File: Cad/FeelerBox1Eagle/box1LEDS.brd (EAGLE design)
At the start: 45 x 70 mm, 20 parts, among them Q3 2N2222A, Q4 2N2222A, Q5 2N2222A, X2 87758-0216

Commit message: fixes0.1
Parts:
- removed CN2: (no value), con-hdrs40:70543-03
- removed Q3, Q4, Q5: 2N2222A, transistor-npn:TO18
- removed R4, R5, R6: (no value), SparkFun-Passives:AXIAL-0.4
- removed X2: 87758-0216, con-molex:87758-0216
- added CN1: (no value), con-hdrs40:SIP-100-2V
- moved R2 22.2 mm to (15.2, 57.1), turned to 90 degrees
- moved R1 13.7 mm to (22.9, 57.1), turned to 90 degrees
- moved R3 6.48 mm to (29.2, 57.1), turned to 90 degrees
- moved U$4 2.54 mm to (22.9, 25.4)
- moved U$5 2.54 mm to (15.2, 25.4)
- moved U$6 2.54 mm to (29.2, 25.4)
- moved U$1 2.54 mm to (22.9, 36.8)
- moved U$2 2.54 mm to (15.2, 36.8)
- moved U$3 2.54 mm to (29.2, 36.8)
- moved U$7 2.54 mm to (22.9, 47.0)
- moved U$8 2.54 mm to (15.2, 47.0)
- moved U$9 2.54 mm to (29.2, 47.0)
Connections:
- removed net D11: CN2.3, R6.P$1
- removed net D13: CN2.1, R4.P$2
- removed net N$29: Q3.3, U$6.1
- removed net N$31: Q4.3, U$5.1
- removed net N$32: Q5.3, U$4.1
- removed net N$6: Q3.1, Q4.1, Q5.1, X2.2
- removed net N$7: Q4.2, R5.P$2
- removed net N$8: CN2.2, R5.P$1
- removed net N$9: Q5.2, R4.P$1
- net N$4: now also CN1.2, U$4.1, U$5.1, U$6.1; no longer Q3.2, R6.P$2
- net N$5: now also CN1.1; no longer X2.1
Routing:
- net N$6: track 106.7 -> 0.00 mm
- net N$5: track 53.5 -> 17.8 mm
- net N$9: track 25.8 -> 0.00 mm
- net N$2: track 23.8 -> 0.00 mm
- net N$7: track 19.1 -> 0.00 mm
- net N$3: track 14.7 -> 0.00 mm
- net N$1: track 8.19 -> 0.00 mm
- net N$32: track 6.11 -> 0.00 mm
- net D13: track 5.66 -> 0.00 mm
- net N$4: track 40.5 -> 46.1 mm
- net N$31: track 5.20 -> 0.00 mm
- net N$29: track 5.20 -> 0.00 mm
- net D11: track 4.34 -> 0.00 mm
- net N$8: track 4.34 -> 0.00 mm

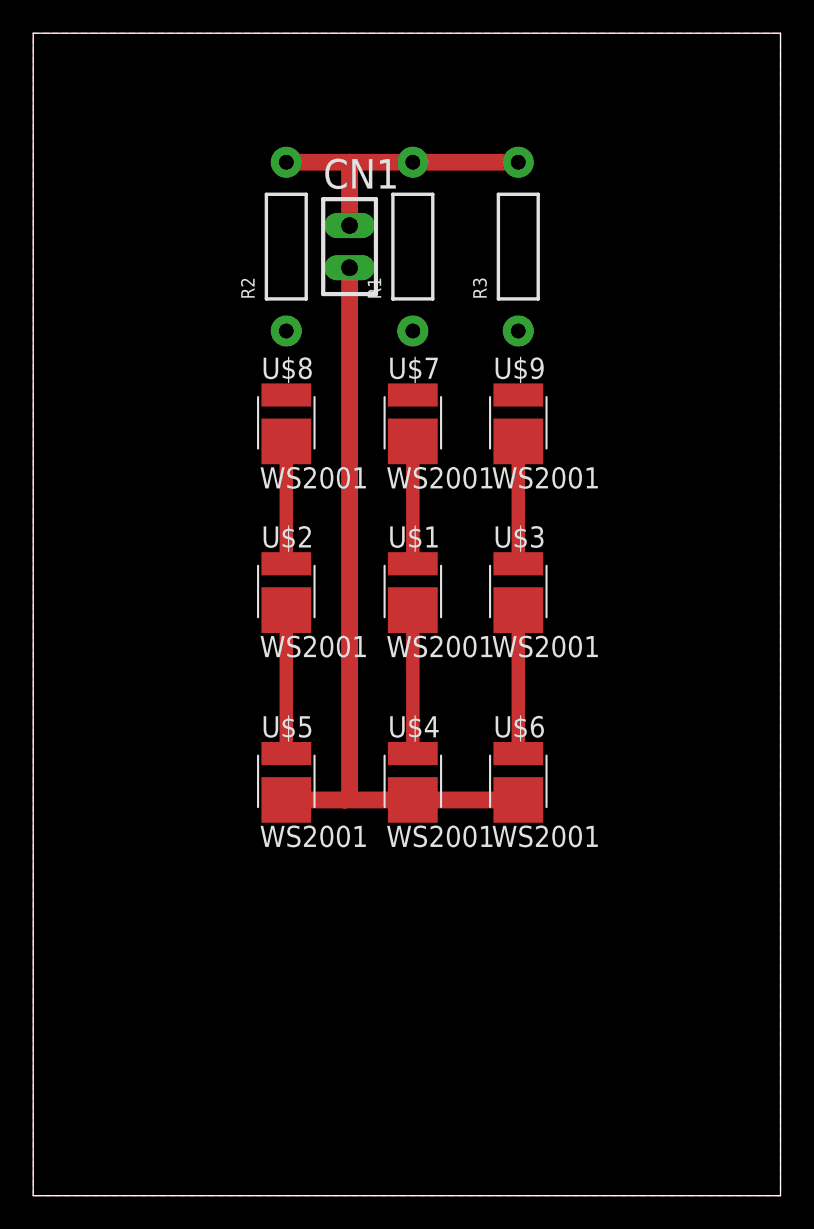
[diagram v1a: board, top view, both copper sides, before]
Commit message: fixes
Fixes, and made made box1Ledboard smaller to improve wifi signal
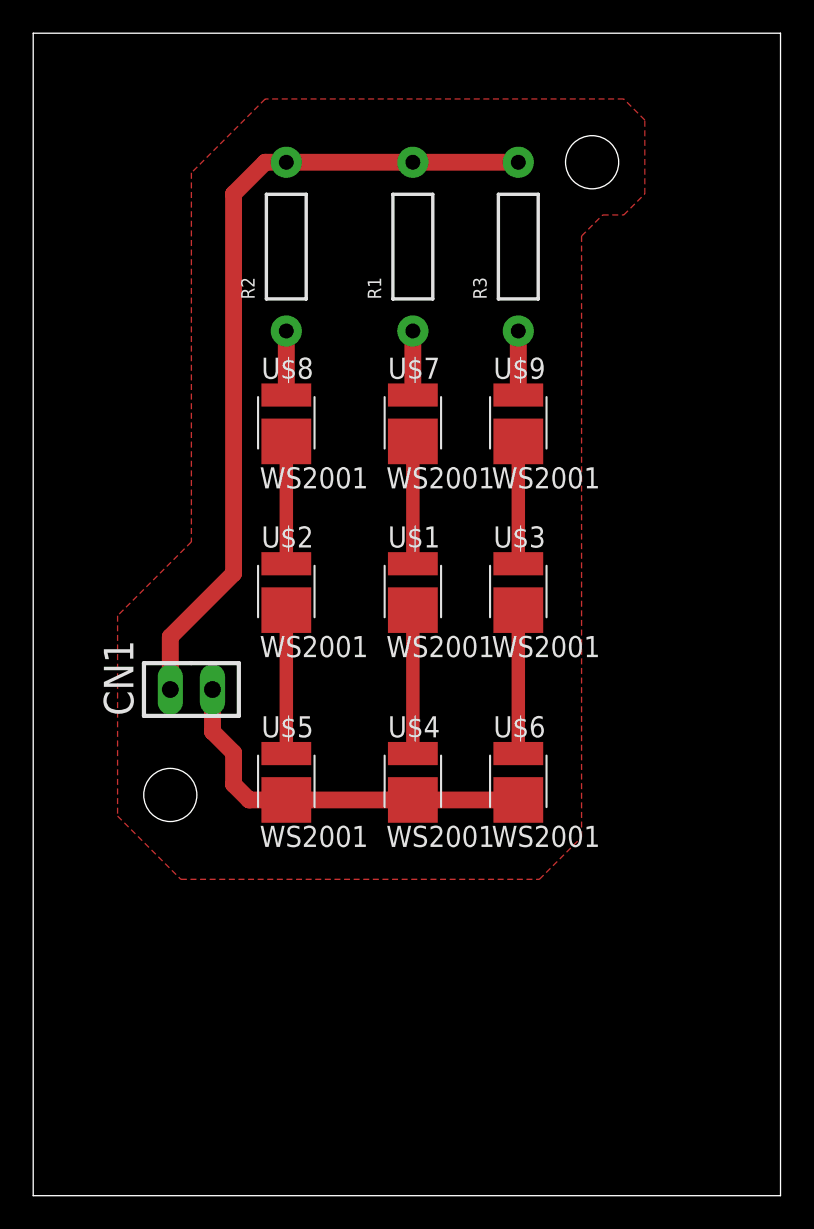
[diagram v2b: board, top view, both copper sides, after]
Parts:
- moved CN1 28.3 mm to (9.53, 30.5), turned to 0 degrees
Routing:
- net N$5: track 17.8 -> 49.4 mm
- net N$4: track 46.1 -> 23.8 mm
- net N$3: track 0.00 -> 3.86 mm
- net N$2: track 0.00 -> 3.86 mm
- net N$1: track 0.00 -> 3.86 mm
- added copper zone on layer 1, net N$6
- removed copper zone on layer 1, net N$10

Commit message: updates
bah
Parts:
- moved CN1 31.0 mm to (21.6, 59.1)
- moved U$5 24.8 mm to (28.6, 46.4)
- moved U$9 21.7 mm to (15.9, 29.8)
- moved U$4 13.9 mm to (28.6, 38.1)
- moved U$2 12.2 mm to (22.9, 46.4)
- moved U$7 11.3 mm to (15.9, 38.1)
- moved U$3 9.44 mm to (22.9, 29.8)
- moved R3 5.43 mm to (24.1, 55.2), turned to 180 degrees
- moved R1 5.24 mm to (24.1, 52.1), turned to 180 degrees
- moved U$6 4.49 mm to (28.6, 29.8)
- moved R2 1.80 mm to (16.5, 55.9)
- moved U$1 1.27 mm to (22.9, 38.1)
- moved U$8 0.90 mm to (15.9, 46.4)
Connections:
- removed net N$20: U$1.2, U$7.1
- removed net N$21: U$2.2, U$8.1
- removed net N$22: U$3.2, U$9.1
- removed net N$23: U$3.1, U$6.2
- removed net N$24: U$2.1, U$5.2
- removed net N$25: U$1.1, U$4.2
- removed net N$4: CN1.2, U$4.1, U$5.1, U$6.1
- new net GND: CN1.2, U$1.1, U$2.1, U$3.1, U$4.1, U$5.1, U$6.1, U$7.1, U$8.1, U$9.1
- net N$1: now also U$3.2, U$6.2
- net N$2: now also U$2.2, U$5.2
- net N$3: now also U$1.2, U$4.2
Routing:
- net GND: track 0.00 -> 93.9 mm
- net N$1: track 3.86 -> 42.5 mm
- net N$5: track 49.4 -> 12.5 mm
- net N$3: track 3.86 -> 28.0 mm
- net N$4: track 23.8 -> 0.00 mm
- net N$2: track 3.86 -> 16.2 mm
- net N$25: track 8.64 -> 0.00 mm
- net N$24: track 8.64 -> 0.00 mm
- net N$23: track 8.64 -> 0.00 mm
- net N$22: track 7.37 -> 0.00 mm
- net N$21: track 7.37 -> 0.00 mm
- net N$20: track 6.40 -> 0.00 mm
- removed copper zone on layer 1, net N$6
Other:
- outline, holes or cut-outs redrawn
